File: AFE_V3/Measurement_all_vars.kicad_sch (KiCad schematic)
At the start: 64 parts, among them IC10 MAX4526EUA+, IC6 LT6372HMSE-1#PBF, IC8 MAX4526EUA+, IC9 MAX4526EUA+, J10 Conn_Coaxial, J11 Conn_Coaxial, J12 Conn_Coaxial, J7 Conn_Coaxial, J8 Conn_Coaxial, J9 Conn_Coaxial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

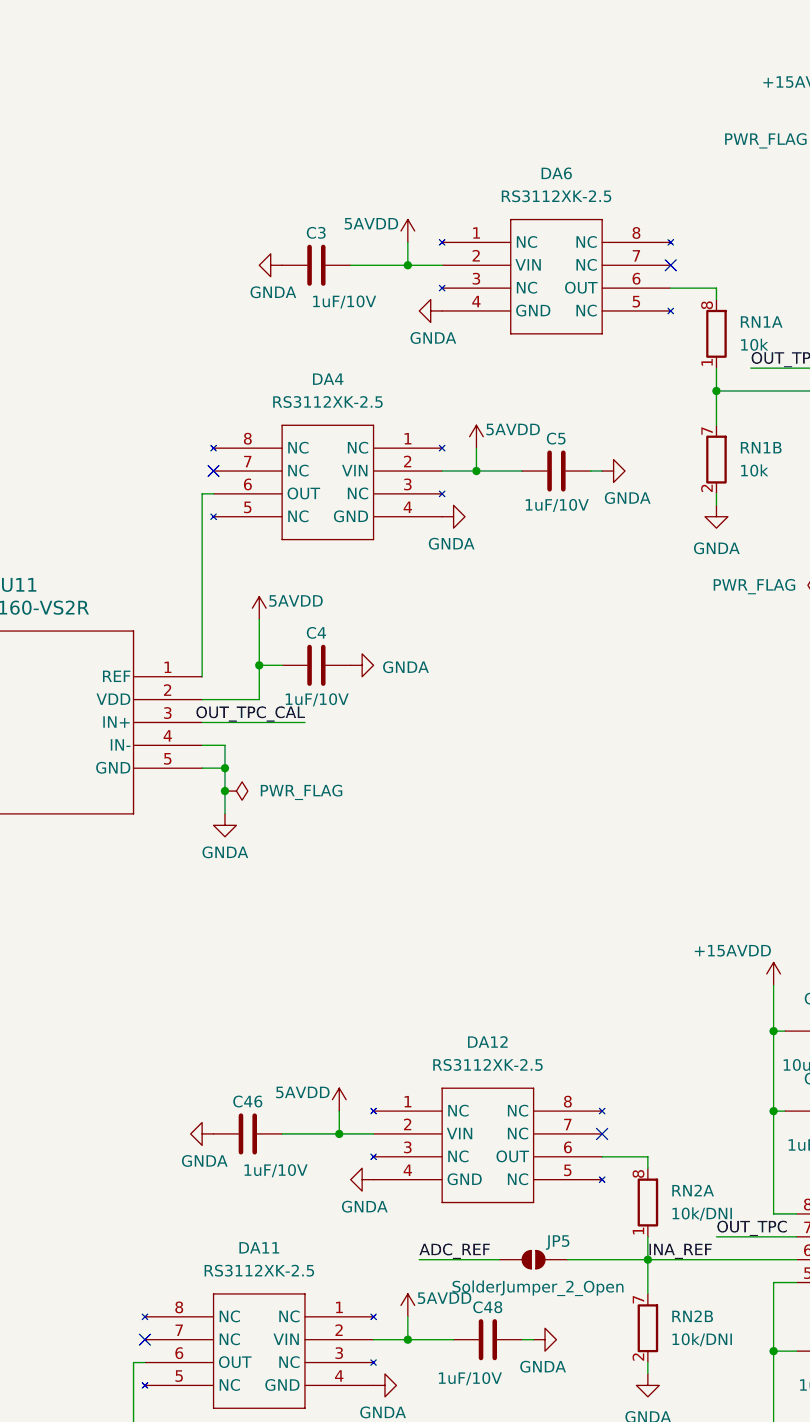
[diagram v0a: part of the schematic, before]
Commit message: PCB tracing in progress. Added some 3d models
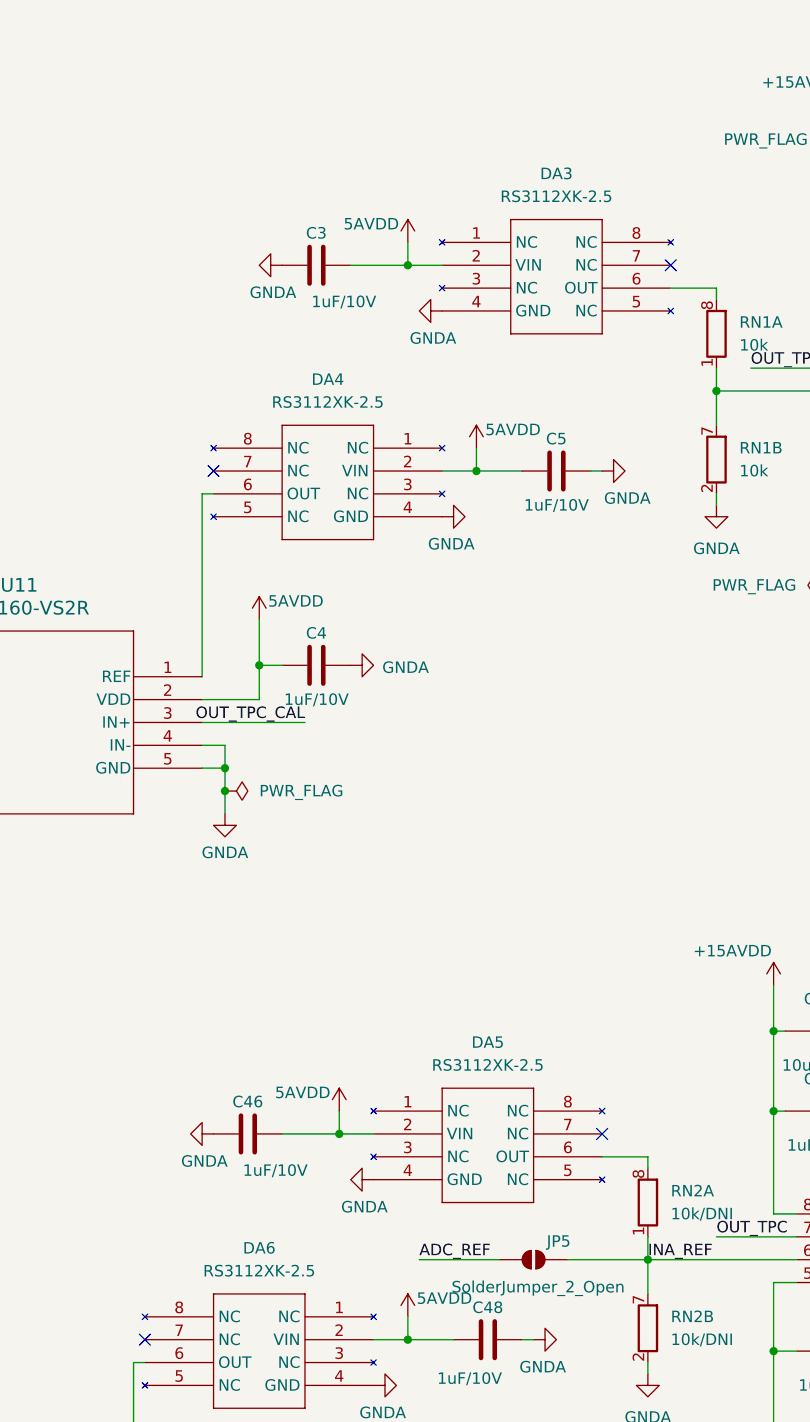
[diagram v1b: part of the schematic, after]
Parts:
- removed DA11, DA12: RS3112XK-2.5, Package_SO:SOIC-8_3.9x4.9mm_P1.27mm, symbol zpc-lib:RS3112
- added DA3, DA5: RS3112XK-2.5, Package_SO:SOIC-8_3.9x4.9mm_P1.27mm, symbol zpc-lib:RS3112
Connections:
- net 5AVDD: now also DA3.2 (VIN), DA5.2 (VIN)
- net ADC_REF: now also DA6.6 (OUT)
- net GNDA: now also DA3.4 (GND), DA5.4 (GND)
- net at RN1.8 (R1.2): now also DA3.6 (OUT); no longer DA6.6 (OUT)
- net at RN2.8 (R1.2): now also DA5.6 (OUT)

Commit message: PCB tracing in progress
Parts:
- removed J10, J11, J12, J7, J8, J9: Conn_Coaxial, Connector_Coaxial:BNC_Amphenol_B6252HB-NPP3G-50_Horizontal, symbol Connector:Conn_Coaxial
- added JP1, JP2, JP3: SolderJumper_2_Open, Jumper:SolderJumper-2_P1.3mm_Open_TrianglePad1.0x1.5mm, symbol Jumper:SolderJumper_2_Open
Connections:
- net GNDA: now also JP2.1 (A); no longer U11.4 (IN-)
- net INA_REF_CAL: now reaches DA2.6 (REF), RN1.1 (R1.1), RN1.7 (R2.2)
- net INA_REF_CAL: now also JP1.2 (B), JP3.1 (A)
- net imp+2: now reaches IC10.2 (B)
- net ADC_REF_CAL: now reaches DA4.6 (OUT), U11.1 (REF)
- net ADC_REF_CAL: now also JP1.1 (A)
- net imp+1: now reaches IC10.1 (A)
- net imp-2: now reaches IC9.2 (B)
- net cur-1: now reaches IC8.1 (A)
- net cur-2: now reaches IC8.2 (B)
- net imp-1: now reaches IC9.1 (A)
- new net: JP2.2 (B), JP3.2 (B), U11.4 (IN-)
